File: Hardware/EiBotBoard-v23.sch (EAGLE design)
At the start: 105 parts, among them IC1 A4983ALT1, IC2 A4983ALT1, IC3 PIC18F46J50-I/PT, IC4 LM317MABDT, IC5 LM317MABDT, J3 USBSMD, J4 IO, J5 IO, J6 POWER_JACKSMD, J7 POWER_JACKSMD, J8 ICSP, SW1 PRG, SW2 RST

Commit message: Version 2.3 from Schmalz Haus. This is the latest version that is in production at SeeedStudios (EMSL) and is shipping with EggBot and WatercolorBot. See changes.txt and schematic for list of changes from v2.1 (the latest version SparkFun is producing as of 3/30/2015) to version 2.3. Also adding BOM in.
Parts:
- removed D4: CGRM4001-G, diode:CGRM4001-G
- removed IC5: LM317MABDT, v-reg:LM317MABDT
- removed J6: POWER_JACKSMD, SparkFun11_03_09:POWER_JACKSMD
- removed JP11: LOGO-SFENEW, SparkFun-12-01-09:LOGO-SFENEW
- removed JP12, JP13: (no value), SparkFun-12-01-09:JUMPER-2SMD-NO
- removed R19: 715, rcl:R-US_R0603
- removed R24: 240, rcl:R-US_R0603
- removed U$10, U$11, U$6, U$7, U$8, U$9: PAD, Testing:PAD
- added LOGO1: OSHW_LOGO_8MILX0100-NT, OSHW:OSHW_LOGO_8MILX0100-NT
- added U1: CJ78M05-1300040P1, OPL Eagle Library:CJ78M05-1300040P1
- C1, C10, C11, C12, C15, C16, C18, C19, C2, C3, C4, C5, C6, C7, C8, C9: device SparkFun-2-11-09:CAP0603 -> OPL Eagle Library:C-0603
- C13, C17: device SparkFun-2-11-09:CAP_POL1206 -> OPL Eagle Library:C-0805
- C14: device SparkFun:CAP_POLG -> SparkFun:CAP_POLD
- C20: value 1uF -> .1uF; device SparkFun-2-11-09:CAP0603 -> OPL Eagle Library:C-0603
- C21: value .1uf -> 1uF; device SparkFun-2-11-09:CAP0603 -> OPL Eagle Library:C-0603
- D1: value (none) -> SS54B; device diode:DIODE-DO214AC -> OPL Eagle Library:D-SMB
- D2, D3: value (none) -> SS0520-7-F; device SparkFun:DIODESMA -> OPL Eagle Library:D-SOD-123
- F1: value PTCSMD -> FUSE-1206, 500mA; device SchmalzHaus:PTCSMD -> OPL Eagle Library:FUSE-1206
- IC1, IC2: value A4983ALT1 -> A4983; device Testing:A4983ALT1 -> SchmalzHaus:A4983
- J3: value USBSMD -> MINI-USB-5P-3400020P1; device SchmalzHaus:USBSMD -> OPL Eagle Library:MINI-USB-5P-3400020P1
- J7: value POWER_JACKSMD -> JACK-DC-3P-3410020P1; device SparkFun11_03_09:POWER_JACKSMD -> OPL Eagle Library:JACK-DC-3P-3410020P1
- JP14, JP15: value FIDUCIALUFIDUCIAL -> FIDUCIAL1X2; device SparkFun:FIDUCIALUFIDUCIAL -> SparkFun:FIDUCIAL1X2
- LED1: value DIR1_RED -> RED; device SparkFun-2-11-09:LED0603 -> OPL Eagle Library:LED
- LED2: value DIR2_RED -> RED; device SparkFun-2-11-09:LED0603 -> OPL Eagle Library:LED
- PWR, USB, USR: device SparkFun-2-11-09:LED0603 -> OPL Eagle Library:LED
- R10, R15, R16, R20, R21, R22, R23, R25, R26, R27, R5, R6, R7, R8, R9: device rcl:R-US_R0603 -> OPL Eagle Library:R-0603
- R12, R14: value 47K -> 4.7K; device rcl:R-US_R0603 -> OPL Eagle Library:R-0603
- R13: value 47K -> 8.2K; device rcl:R-US_R0603 -> OPL Eagle Library:R-0603
- R17: value 68.1K -> 8.2K; device rcl:R-US_R0603 -> OPL Eagle Library:R-0603
- R18: value 4.7K -> 1K; device rcl:R-US_R0603 -> OPL Eagle Library:R-0603
- renumbered 2MM1 to J1, 2MM2 to J2
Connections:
- removed net 5V_ALT: C20.2, IC5.OUT, JP13.1, R24.2
- removed net N$12: IC1.NC@2, U$11.P$1
- removed net N$13: IC1.NC@3, U$10.P$1
- removed net N$14: IC2.NC@1, U$6.P$1
- removed net N$15: IC2.NC@2, U$7.P$1
- removed net N$18: IC2.NC@3, U$8.P$1
- removed net N$26: LED2.C, R16.2
- removed net N$27: PWR.A, R20.1
- removed net N$29: R26.1, USB.A
- removed net N$30: R25.1, USR.A
- removed net N$35: LED1.C, R15.2
- new net N$1: LED2.-, R16.2
- net 3.3V: now also C17.2, PWR.+; no longer C17.+, R20.2
- net 5V_SVO: now also C20.2, U1.OUT; no longer JP12.2, JP13.2
- net D+: now also J3.DP; no longer J3.D+
- net D-: now also J3.DM; no longer J3.D-
- net DIR_1: now also LED1.+; no longer LED1.A
- net DIR_2: now also LED2.+; no longer LED2.A
- net GND: now also C13.1, C17.1, J3.GND@3, J3.GND@4, J3.GND@5, J7.-, R20.1, R25.1, R26.1, U1.GND; no longer C13.-, C17.-, J3.GND, J6.GND, J6.GNDBREAK, J7.GND, J7.GNDBREAK, PWR.C, R19.2, USB.C, USR.C
- net N$10: now also R25.2, USR.-; no longer D4.C, JP12.1
- net N$11: now also PWR.-, R20.2; no longer IC1.NC@1, U$9.P$1
- net N$2: now also D2.-, D3.-; no longer D2.C, D3.C
- net N$6: now also D1.+, J7.+; no longer D1.A, J7.PWR
- net N$7: now also LED1.-, R15.2; no longer D4.A, J6.PWR
- net N$8: now also R26.2, USB.-; no longer IC5.ADJ, R19.1, R24.1
- net USB_LED: now also USB.+; no longer R26.2
- net USR_LED: now also USR.+; no longer R25.2
- net V+: now also D1.-, D2.+, U1.IN; no longer D1.C, D2.A, IC5.IN
- net VBUS: now also D3.+, J3.VCC; no longer D3.A, J3.VBUS
- net VCAP: now also C13.2; no longer C13.+
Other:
- note added: "0.0V aprox 0mA"
- note added: "1.8V approx 1A"
- note added: "3.3V approx 1.88A"
- note added: "9V to 25V DC"
- note added: "Added big EBB silk text"
- note added: "All screws holes now ringed by GND"
- note added: "DIR1 RED"
- note added: "DIR2 RED"
- note added: "Increased copper areas under power and USB jacks for physical stability"
- note added: "Made most silk .04 high, fixed silk placement extra I/O"
- note added: "Must be at LEAST 35V"
- note added: "PWR GREEN"
- note added: "R17 changed to 68K to provide solid HIGH for USB detect"
- note added: "Re-oriented silk text to be equally wrong for EggBot and WaterColorBot"
- note added: "Removed separate servo power supply from bottom of board."
- note added: "Replaced all possible parts with SeeedStudio OPL replacements"
- note added: "Replaced directional arrow for CUR ADJ pot with phyiscal locator"
- note added: "Rotated all silk text for EggBot orientation"
- note added: "Rounderd corners"
- note added: "USB Connector"
- note added: "USB GREEN"
- note added: "USR RED"
- note added: "Updated R12,R17, R13, R14, R18 to be OPL values"
- note added: "V+ can see up to 25V, so R1/R4 divides"
- note added: "Version 2.3, 09/15/2013"
- note added: "copyright 2011-2013"
- note added: "it down so 25V on V+ shows up as 2.717V"
- note added: "phases. From 0mA to about 1.25A per"
- note added: "v2.1 11/22/2010"
- note added: "v2.2 08/20/2011"
- note added: "v2.3 09/15/2013"
- note removed: "-moved some vias as necessary"
- note removed: "-replaced two driver IC footprints with 1:1 rev"
- note removed: "-routed all traces directly away from those ICs"
- note removed: "0.0V 46mA"
- note removed: "2.58V 1.35A"
- note removed: "9V to 30V DC"
- note removed: "Alt Servo Power"
- note removed: "Changed value on R17 from 47K to 68K"
- note removed: "Cut JP13 and bridge JP12"
- note removed: "Green"
- note removed: "J3"
- note removed: "Must be at LEAST 30V"
- note removed: "Red"
- note removed: "The IO RC17 on the pic is a Schmidt trigger input and needs 0.8 * Vdd,"
- note removed: "This is necessary to trigger the IO threshold of 3V"
- note removed: "Updates on v23: (1/5/12 Theo)"
- note removed: "V+ can see up to 37V, so R1/R4 divides"
- note removed: "Version 2.2, 11/19/2010"
- note removed: "and add D4 and J6 to enable"
- note removed: "because only 2-layer board"
- note removed: "external RC servo power"
- note removed: "it down so 37V on V+ shows up as 3.36V"
- note removed: "phases. From 46mA to 1.25A per"
- note removed: "v2.2 11/19/2010"
- note removed: "which is 2.65V as a minimum HIGH threshold"
- moved on the sheet: IC1, IC2

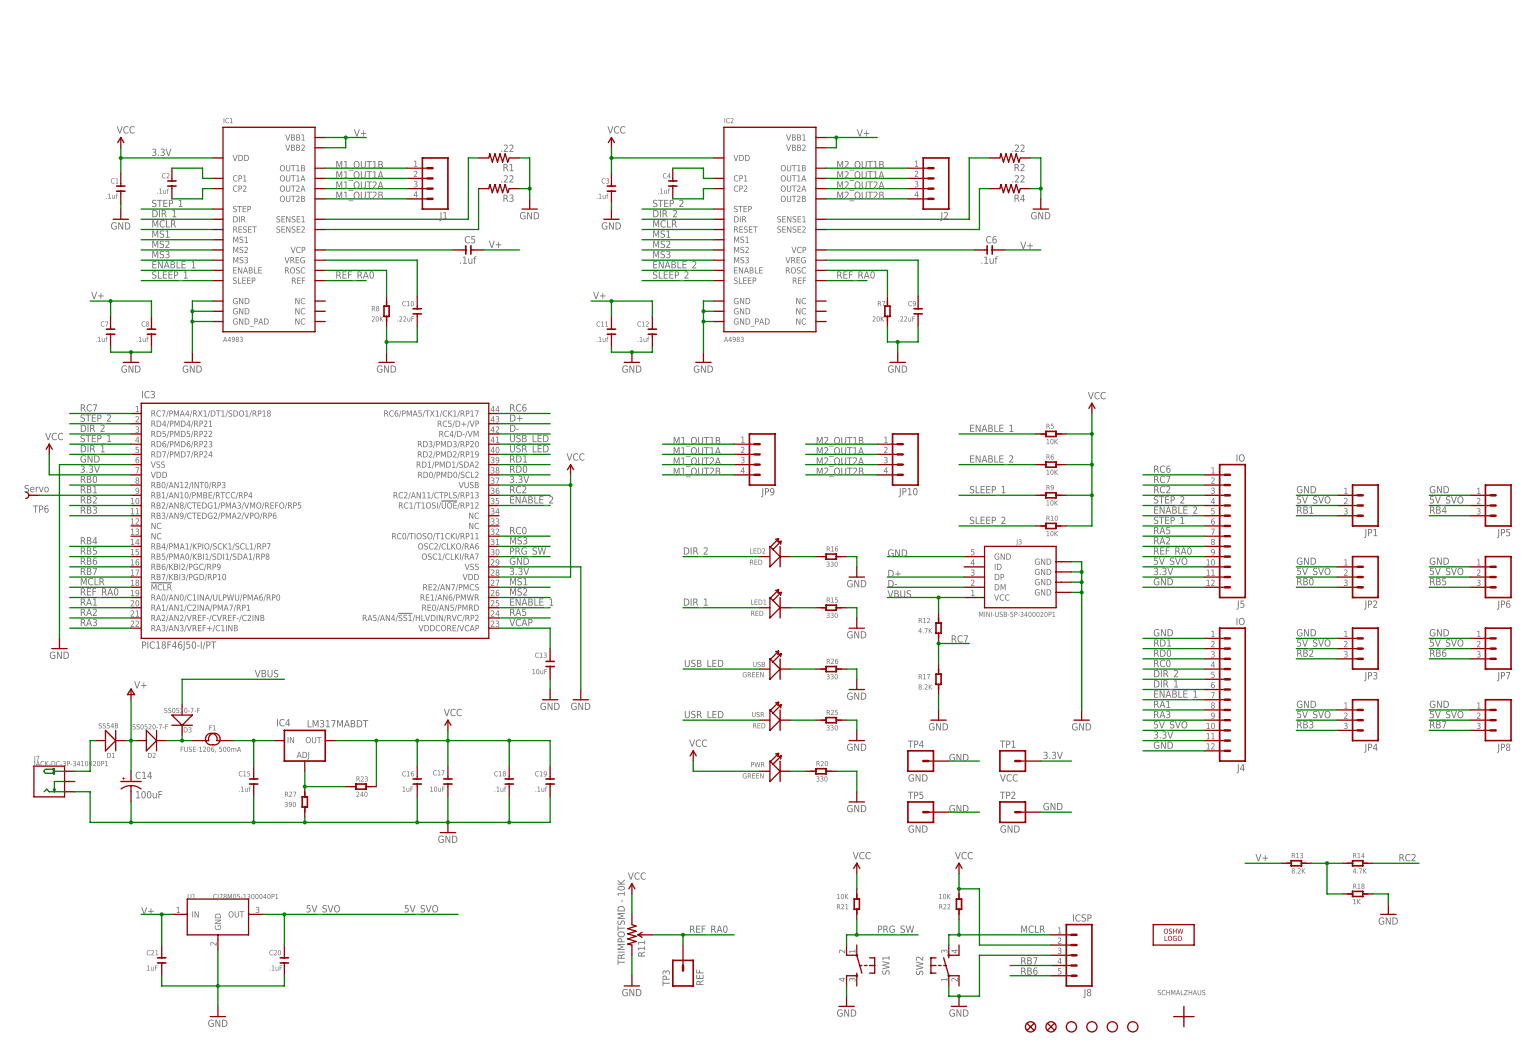
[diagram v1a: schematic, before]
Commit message: Updating part numbers to SFE libraries, swapping vregs
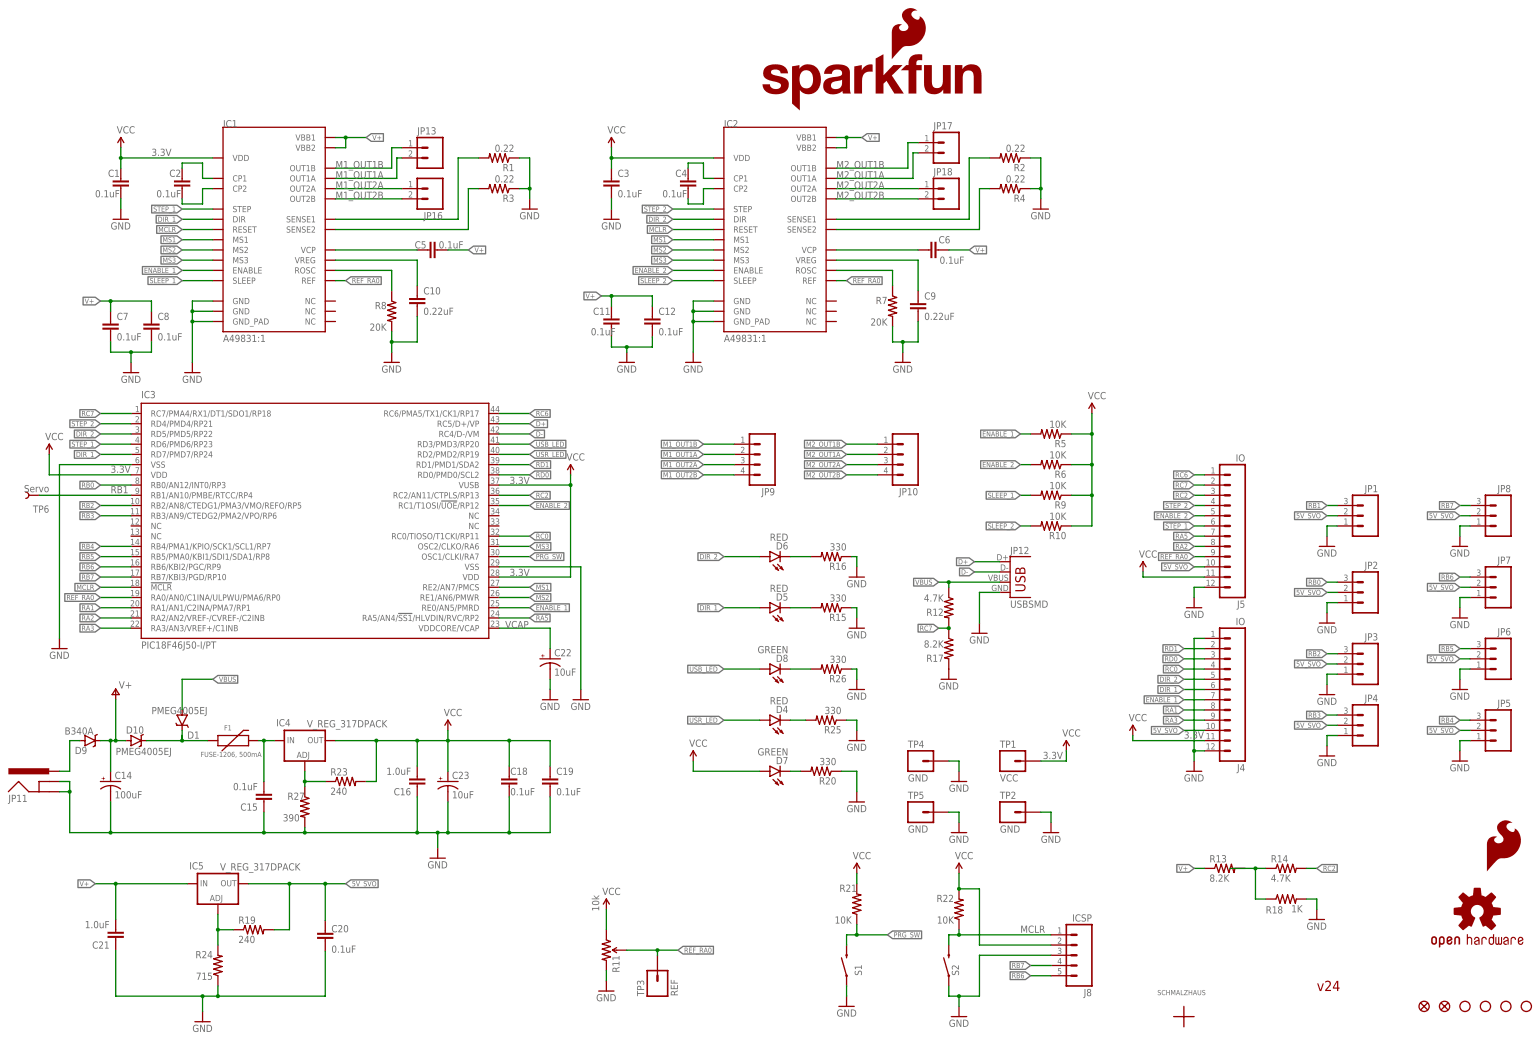
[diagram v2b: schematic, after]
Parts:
- removed C13, C17: 10uF, OPL Eagle Library:C-0805
- removed D2, D3: SS0520-7-F, OPL Eagle Library:D-SOD-123
- removed J1, J2: (no value), EiBotBoard-v21:SCHMALZHAUS_M04
- removed J3: MINI-USB-5P-3400020P1, OPL Eagle Library:MINI-USB-5P-3400020P1
- removed J7: JACK-DC-3P-3410020P1, OPL Eagle Library:JACK-DC-3P-3410020P1
- removed LED1, LED2, USR: RED, OPL Eagle Library:LED
- removed PWR, USB: GREEN, OPL Eagle Library:LED
- removed SW1: PRG, SparkFunEagle-6-6-07:TAC_SWITCHSND
- removed SW2: RST, SparkFunEagle-6-6-07:TAC_SWITCHSND
- removed U1: CJ78M05-1300040P1, OPL Eagle Library:CJ78M05-1300040P1
- added C22, C23: 10uF, SparkFun-Capacitors:10UF-16V-10%(TANT)
- added D10: PMEG4005EJ, SparkFun-DiscreteSemi:DIODE-SCHOTTKY-PMEG4005EJ
- added D4, D5, D6: RED, SparkFun-LED:LED-RED0603
- added D7, D8: GREEN, SparkFun-LED:LED-GREEN0603
- added D9: B340A, SparkFun-DiscreteSemi:DIODE-SCHOTTKY-B340A
- added IC5: V_REG_317DPACK, SparkFun-PowerIC:V_REG_317DPACK
- added JP11: POWER_JACKPTH_LOCK, SparkFun-Connectors:POWER_JACKPTH_LOCK
- added JP12: USBSMD, SparkFun-Connectors:USBSMD
- added JP13, JP16, JP17, JP18: (no value), SparkFun-Connectors:M023.5MM_LOCK
- added LOGO2: SFE_LOGO_FLAME.2_INCH, SparkFun-Aesthetics:SFE_LOGO_FLAME.2_INCH
- added LOGO3: SFE_LOGO_NAME_FLAME.2_INCH, SparkFun-Aesthetics:SFE_LOGO_NAME_FLAME.2_INCH
- added R19: 240, SparkFun-Resistors:240OHM1/10W1%(0603)
- added R24: 715, SparkFun-Resistors:715OHM1/10W1%(0603)
- added S1, S2: SWITCH-MOMENTARY-2SMD, SparkFun-Electromechanical:SWITCH-MOMENTARY-2SMD
- C1, C11, C12, C15, C18, C19, C2, C3, C4, C5, C6, C7, C8: value .1uf -> 0.1uF; device OPL Eagle Library:C-0603 -> SparkFun-Capacitors:0.1UF-100V-10%(0603)
- C10, C9: value .22uF -> 0.22uF; device OPL Eagle Library:C-0603 -> SparkFun-Capacitors:0.22UF50V-20%,+80%(0603)
- C14: device SparkFun:CAP_POLD -> SparkFun-Capacitors:100UF-63V-20%(ELECT)
- C16, C21: value 1uF -> 1.0uF; device OPL Eagle Library:C-0603 -> SparkFun-Capacitors:1.0UF-16V-10%(0603)
- C20: value .1uF -> 0.1uF; device OPL Eagle Library:C-0603 -> SparkFun-Capacitors:0.1UF-100V-10%(0603)
- D1: value SS54B -> PMEG4005EJ; device OPL Eagle Library:D-SMB -> SparkFun-DiscreteSemi:DIODE-SCHOTTKY-PMEG4005EJ
- F1: device OPL Eagle Library:FUSE-1206 -> SparkFun-PowerIC:PTCTHERMISTOR1206
- IC1, IC2: value A4983 -> A49831:1; device SchmalzHaus:A4983 -> SparkFun-PowerIC:A49831:1
- IC3: device SchmalzHaus:PIC18F4J50 -> Testing:PIC18F4J50
- IC4: value LM317MABDT -> V_REG_317DPACK; device v-reg:LM317MABDT -> SparkFun-PowerIC:V_REG_317DPACK
- J4, J5: device SparkFun-12-01-09:M12PTH -> SparkFun-Connectors:M12PTH
- J8: device SchmalzHaus:M05_WIDENOSILK -> SparkFun-Connectors:M05NO_SILK
- JP1: device SparkFun:M03LOCK_NO_SILK -> SparkFun-Connectors:M03LOCK_NO_SILK
- JP10, JP9: device SparkFun-12-01-09:M04POLAR -> SparkFun-Connectors:M04POLAR
- JP14, JP15: device SparkFun:FIDUCIAL1X2 -> SparkFun-Aesthetics:FIDUCIAL1X2
- JP2, JP3, JP4, JP5, JP6, JP7, JP8: device SparkFun-12-01-09:M031X03_NO_SILK -> SparkFun-Connectors:M03LOCK_NO_SILK
- LOGO1: value OSHW_LOGO_8MILX0100-NT -> OSHW-LOGOS; device OSHW:OSHW_LOGO_8MILX0100-NT -> SparkFun-Aesthetics:OSHW-LOGOS
- R1, R2, R3, R4: value .22 -> 0.22; device rcl:R-US_R0805 -> SparkFun-Resistors:0.22OHM-1/4W-1%(0805)
- R10, R21, R22, R5, R6, R9: device OPL Eagle Library:R-0603 -> SparkFun-Resistors:10KOHM-1/10W-1%(0603)0603
- R11: value TRIMPOTSMD - 10K -> 10k; device SparkFun11_03_09:TRIMPOTSMD -> SparkFun-Electromechanical:TRIMPOTRES-09285
- R12, R14: device OPL Eagle Library:R-0603 -> SparkFun-Resistors:4.7KOHM-1/10W-1%(0603)
- R13, R17: device OPL Eagle Library:R-0603 -> SparkFun-Resistors:8.2KOHM-1/10W-5%(0603)
- R15, R16, R20, R25, R26: device OPL Eagle Library:R-0603 -> SparkFun-Resistors:330OHM1/10W1%(0603)
- R18: device OPL Eagle Library:R-0603 -> SparkFun-Resistors:1KOHM-1/10W-1%(0603)
- R23: device OPL Eagle Library:R-0603 -> SparkFun-Resistors:240OHM1/10W1%(0603)
- R27: device OPL Eagle Library:R-0603 -> SparkFun-Resistors:390OHM1/10W1%(0603)
- R7, R8: device OPL Eagle Library:R-0603 -> SparkFun-Resistors:20KOHM1/10W5%(0603)
- TP3: device SchmalzHaus:M01PTH -> SparkFun-Connectors:M01PTH
- TP6: device SparkFun:TEST-POINT3X5 -> SparkFun-Passives:TEST-POINT3X5
- U$2, U$3, U$4, U$5: device SparkFun01082009:STAND-OFF -> SparkFun-Electromechanical:STAND-OFF
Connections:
- new net N$12: IC5.ADJ, R19.1, R24.2
- net 3.3V: now also C23.+, D7.A; no longer C17.2, PWR.+
- net 5V_SVO: now also IC5.OUT, R19.2; no longer U1.OUT
- net D+: now also JP12.D+; no longer J3.DP
- net D-: now also JP12.D-; no longer J3.DM
- net DIR_1: now also D5.A; no longer LED1.+
- net DIR_2: now also D6.A; no longer LED2.+
- net GND: now also C22.-, C23.-, JP11.GND, JP11.GNDBREAK, JP12.GND, R24.1, S1.1, S2.1; no longer C13.1, C17.1, J3.GND@1, J3.GND@2, J3.GND@3, J3.GND@4, J3.GND@5, J7.-, SW1.4, SW2.1, U1.GND
- net M1_OUT1A: now also JP13.2; no longer J1.2
- net M1_OUT1B: now also JP13.1; no longer J1.1
- net M1_OUT2A: now also JP16.1; no longer J1.3
- net M1_OUT2B: now also JP16.2; no longer J1.4
- net M2_OUT1A: now also JP17.2; no longer J2.2
- net M2_OUT1B: now also JP17.1; no longer J2.1
- net M2_OUT2A: now also JP18.1; no longer J2.3
- net M2_OUT2B: now also JP18.2; no longer J2.4
- net MCLR: now also S2.2; no longer SW2.3
- net N$1: now also D6.C; no longer LED2.-
- net N$10: now also D4.C; no longer USR.-
- net N$11: now also D7.C; no longer PWR.-
- net N$2: now also D1.C, D10.C; no longer D2.-, D3.-
- net N$6: now also D9.A, JP11.PWR; no longer D1.+, J7.+
- net N$7: now also D5.C; no longer LED1.-
- net N$8: now also D8.C; no longer USB.-
- net PRG_SW: now also S1.2; no longer SW1.2
- net USB_LED: now also D8.A; no longer USB.+
- net USR_LED: now also D4.A; no longer USR.+
- net V+: now also D10.A, D9.C, IC5.IN; no longer D1.-, D2.+, U1.IN
- net VBUS: now also D1.A, JP12.VBUS; no longer D3.+, J3.VCC
- net VCAP: now also C22.+; no longer C13.2
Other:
- note added: "0.0V approx 0mA"
- note added: "Version 2.4,04/01/2015"
- note added: "v24"
- note removed: "0.0V aprox 0mA"
- note removed: "Version 2.3, 09/15/2013"
- moved on the sheet: C14, IC1, IC2, JP1, JP2, JP3, JP4, JP5, JP6, JP7, JP8, R11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

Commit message: Updating to A4988 ICs
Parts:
- IC1, IC2: value A49831:1 -> A4988ALT1; device SparkFun-PowerIC:A49831:1 -> SparkFun-PowerIC:A4988ALT1
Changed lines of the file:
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@@
 <setting verticaltext="up"/>
 </settings>
-<grid distance="0.05" unitdist="inch" unit="inch" style="lines" multiple="1" display="no" altdistance="0.01" altunitdist="inch" altunit="inch"/>
+<grid distance="0.1" unitdist="inch" unit="inch" style="lines" multiple="1" display="no" altdistance="0.01" altunitdist="inch" altunit="inch"/>
 <layers>
 <layer number="1" name="Top" color="4" fill="1" visible="no" active="no"/>
@@
 <part name="JP2" library="SparkFun-Connectors" deviceset="M03" device="LOCK_NO_SILK"/>
 <part name="R11" library="SparkFun-Electromechanical" deviceset="TRIMPOT" device="RES-09285" value="10k"/>
-<part name="IC1" library="SparkFun-PowerIC" deviceset="A4983" device="1:1"/>
-<part name="IC2" library="SparkFun-PowerIC" deviceset="A4983" device="1:1"/>
+<part name="IC1" library="SparkFun-PowerIC" deviceset="A4988" device="ALT1"/>
+<part name="IC2" library="SparkFun-PowerIC" deviceset="A4988" device="ALT1"/>
 <part name="GND1" library="SparkFun-Aesthetics" deviceset="GND" device=""/>
 <part name="R8" library="SparkFun-Resistors" deviceset="20KOHM1/10W5%(0603)" device="" value="20K"/>

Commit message: Updating additional packages, fixing DRC errors
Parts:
- D1, D10: value PMEG4005EJ -> MBRA140; device SparkFun-DiscreteSemi:DIODE-SCHOTTKY-PMEG4005EJ -> SparkFun-DiscreteSemi:DIODE-SCHOTTKY-MBRA140
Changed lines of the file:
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@@
 <part name="S2" library="SparkFun-Electromechanical" deviceset="SWITCH-MOMENTARY-2" device="SMD"/>
 <part name="D9" library="SparkFun-DiscreteSemi" deviceset="DIODE-SCHOTTKY" device="-B340A" value="B340A"/>
-<part name="D1" library="SparkFun-DiscreteSemi" deviceset="DIODE-SCHOTTKY" device="-PMEG4005EJ" value="PMEG4005EJ"/>
-<part name="D10" library="SparkFun-DiscreteSemi" deviceset="DIODE-SCHOTTKY" device="-PMEG4005EJ" value="PMEG4005EJ"/>
+<part name="D1" library="SparkFun-DiscreteSemi" deviceset="DIODE-SCHOTTKY" device="-MBRA140" value="MBRA140"/>
+<part name="D10" library="SparkFun-DiscreteSemi" deviceset="DIODE-SCHOTTKY" device="-MBRA140" value="MBRA140"/>
 <part name="P+7" library="SparkFun-Aesthetics" deviceset="VCC" device=""/>
 <part name="P+8" library="SparkFun-Aesthetics" deviceset="VCC" device=""/>
